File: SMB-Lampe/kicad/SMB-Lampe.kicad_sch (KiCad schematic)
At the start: 2 parts, among them SW1 SW_SPST, U1 MOUDLE-SEEEDUINO-XIAO-ESP32C3

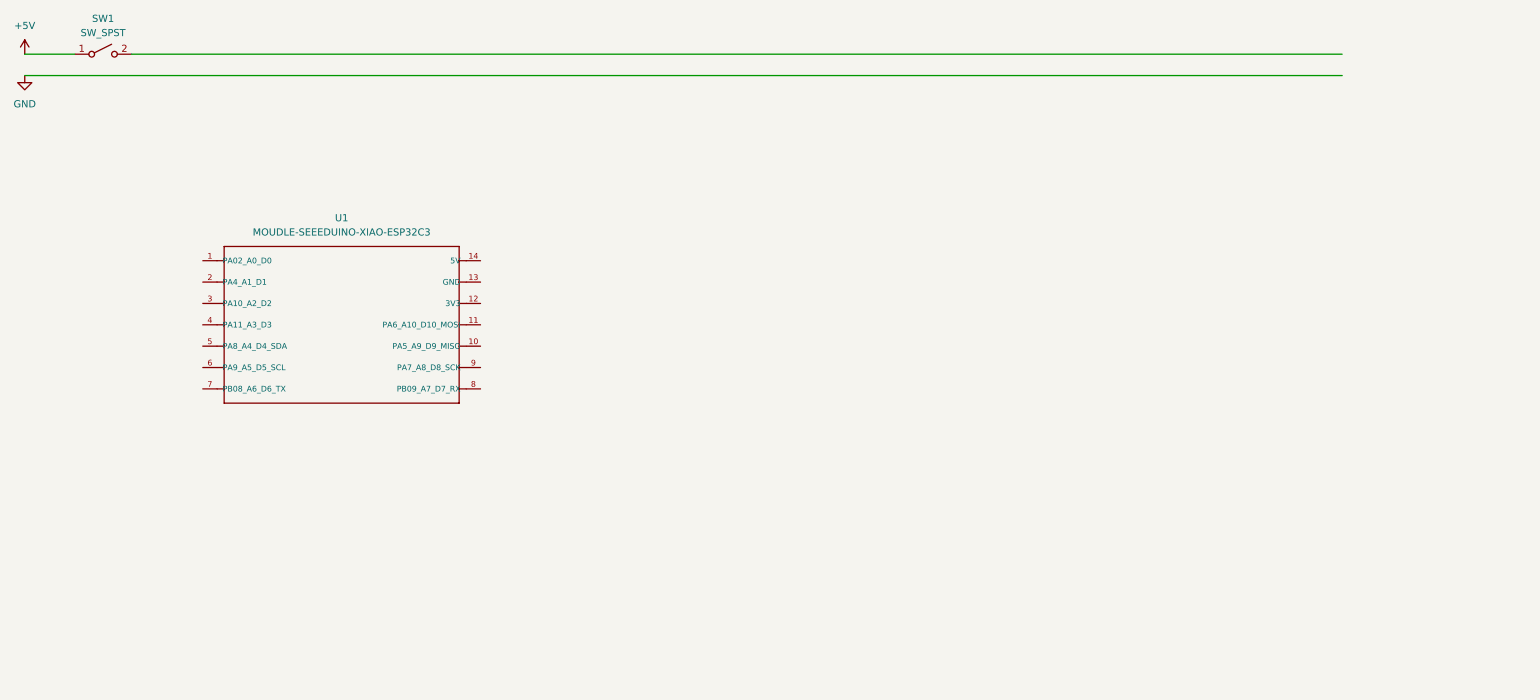
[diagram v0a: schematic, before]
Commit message: Spannungsversorgung zu ESP hinzugefügt
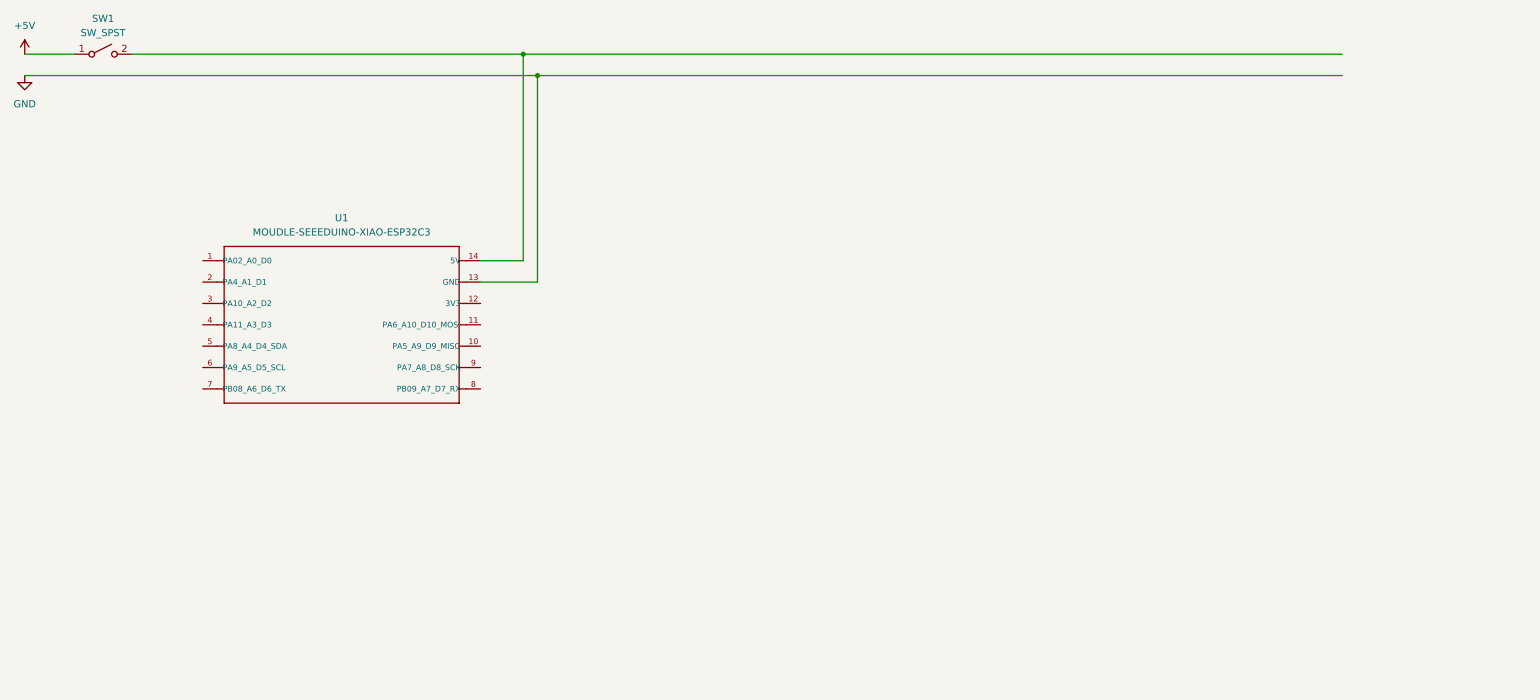
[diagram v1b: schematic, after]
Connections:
- net GND: now also U1.13 (GND)
- net at SW1.2 (B): now also U1.14 (5V)
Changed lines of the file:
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@@
 	(generator_version "9.0")
 	(paper "A4")
+	(junction
+		(at 116.84 29.21)
+		(diameter 0)
+		(color 0 0 0 0)
+	)
+	(junction
+		(at 114.3 25.4)
+		(diameter 0)
+		(color 0 0 0 0)
+	)
 	(wire
 		(pts
@@
 	(wire
 		(pts
-			(xy 25.4 29.21) (xy 260.35 29.21)
+			(xy 114.3 25.4) (xy 114.3 62.23)
 		)
 		(stroke
@@
 	(wire
 		(pts
-			(xy 44.45 25.4) (xy 260.35 25.4)
+			(xy 106.68 66.04) (xy 116.84 66.04)
 		)
 		(stroke
+			(width 0)
+			(type default)
+		)
+	)
+	(wire
+		(pts
+			(xy 116.84 29.21) (xy 260.35 29.21)
+		)
+		(stroke
+			(width 0)
+			(type default)
+		)
+	)
+	(wire
+		(pts
+			(xy 25.4 29.21) (xy 116.84 29.21)
+		)
+		(stroke
+			(width 0)
+			(type default)
+		)
+	)
+	(wire
+		(pts
+			(xy 44.45 25.4) (xy 114.3 25.4)
+		)
+		(stroke
+			(width 0)
+			(type default)
+		)
+	)
+	(wire
+		(pts
+			(xy 106.68 62.23) (xy 114.3 62.23)
+		)
+		(stroke
+			(width 0)
+			(type default)
+		)
+	)
+	(wire
+		(pts
+			(xy 114.3 25.4) (xy 260.35 25.4)
+		)
+		(stroke
+			(width 0)
+			(type default)
+		)
+	)
+	(wire
+		(pts
+			(xy 116.84 29.21) (xy 116.84 66.04)
+		)
+		(stroke

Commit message: Beidseitige Platine Für hinteres Hinterbein
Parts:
- removed U1: MOUDLE-SEEEDUINO-XIAO-ESP32C3, xiao ESP32C3_PCB:MOUDLE14P-SMD-2.54-21X17.8MM, symbol MOUDLE-SEEEDUINO-XIAO-ESP32C3:MOUDLE-SEEEDUINO-XIAO-ESP32C3
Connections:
- net Hinterbein_hinten_Seite1_LED-P/+5V: now reaches SW1.2 (B)
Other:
- added sheet Hauptplatine (Hauptplatine/Hauptplatine.kicad_sch)
- added sheet Hinterbein_hinten_Seite1_LED-P (Hinterbein_hinten_Seite1_LED-P/Hinterbein_hinten_Seite1_LED-P.kicad_sch)
- added sheet Hinterbein_vorne_Seite1_LED-P (Hinterbein_vorne_Seite1_LED-P/Hinterbein_vorne_Seite1_LED-P.kicad_sch)
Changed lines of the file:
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@@
 	(paper "A4")
 	(junction
-		(at 116.84 29.21)
+		(at 101.6 25.4)
 		(diameter 0)
 		(color 0 0 0 0)
 	)
 	(junction
-		(at 114.3 25.4)
+		(at 110.49 58.42)
 		(diameter 0)
 		(color 0 0 0 0)
@@
 	(wire
 		(pts
+			(xy 101.6 25.4) (xy 260.35 25.4)
+		)
+		(stroke
+			(width 0)
+			(type default)
+		)
+	)
+	(wire
+		(pts
 			(xy 25.4 25.4) (xy 34.29 25.4)
 		)
@@
 	(wire
 		(pts
-			(xy 114.3 25.4) (xy 114.3 62.23)
-		)
-		(stroke
-			(width 0)
-			(type default)
-		)
-	)
-	(wire
-		(pts
-			(xy 106.68 66.04) (xy 116.84 66.04)
-		)
-		(stroke
-			(width 0)
-			(type default)
-		)
-	)
-	(wire
-		(pts
-			(xy 116.84 29.21) (xy 260.35 29.21)
-		)
-		(stroke
-			(width 0)
-			(type default)
-		)
-	)
-	(wire
-		(pts
-			(xy 25.4 29.21) (xy 116.84 29.21)
-		)
-		(stroke
-			(width 0)
-			(type default)
-		)
-	)
-	(wire
-		(pts
-			(xy 44.45 25.4) (xy 114.3 25.4)
-		)
-		(stroke
-			(width 0)
-			(type default)
-		)
-	)
-	(wire
-		(pts
-			(xy 106.68 62.23) (xy 114.3 62.23)
-		)
-		(stroke
-			(width 0)
-			(type default)
-		)
-	)
-	(wire
-		(pts
-			(xy 114.3 25.4) (xy 260.35 25.4)
-		)
-		(stroke
-			(width 0)
-			(type default)
-		)
-	)
-	(wire
-		(pts
-			(xy 116.84 29.21) (xy 116.84 66.04)
+			(xy 101.6 25.4) (xy 101.6 58.42)
+		)
+		(stroke
+			(width 0)
+			(type default)
+		)
+	)
+	(wire
+		(pts
+			(xy 25.4 29.21) (xy 260.35 29.21)
+		)
+		(stroke
+			(width 0)
+			(type default)
+		)
+	)
+	(wire
+		(pts
+			(xy 110.49 58.42) (xy 111.76 58.42)
+		)
+		(stroke
+			(width 0)
+			(type default)
+		)
+	)
+	(wire
+		(pts
+			(xy 44.45 25.4) (xy 101.6 25.4)
+		)
+		(stroke
+			(width 0)
+			(type default)
+		)
+	)
+	(wire
+		(pts
+			(xy 101.6 58.42) (xy 110.49 58.42)
 		)
 		(stroke
@@
 		)
 	)
-	(symbol
-		(lib_id "MOUDLE-SEEEDUINO-XIAO-ESP32C3:MOUDLE-SEEEDUINO-XIAO-ESP32C3")
-		(at 82.55 73.66 0)
-		(unit 1)
-		(exclude_from_sim no)
-		(in_bom yes)
-		(on_board yes)
-		(dnp no)
-		(fields_autoplaced yes)
-		(property "Reference" "U1"
-			(at 81.915 54.61 0)
-			(effects
-				(font
-					(size 1.27 1.27)
-				)
-			)
-		)
-		(property "Value" "MOUDLE-SEEEDUINO-XIAO-ESP32C3"
-			(at 81.915 57.15 0)
-			(effects
-				(font
-					(size 1.27 1.27)
-				)
-			)
-		)
-		(property "Footprint" "xiao ESP32C3_PCB:MOUDLE14P-SMD-2.54-21X17.8MM"
-			(at 82.55 73.66 0)
-			(effects
-				(font
-					(size 1.27 1.27)
-				)
-				(justify bottom)
-				(hide yes)
-			)
-		)
-		(property "Datasheet" ""
-			(at 82.55 73.66 0)
-			(effects
-				(font
-					(size 1.27 1.27)
-				)
-				(hide yes)
-			)
-		)
-		(property "Description" ""
-			(at 82.55 73.66 0)
-			(effects
-				(font
-					(size 1.27 1.27)
-				)
-				(hide yes)
-			)
-		)
-		(pin "14"
-		)
-		(pin "10"
-		)
-		(pin "4"
-		)
-		(pin "12"
-		)
-		(pin "13"
-		)
-		(pin "2"
-		)
-		(pin "3"
-		)
-		(pin "5"
-		)
-		(pin "7"
-		)
-		(pin "8"
-		)
-		(pin "9"
-		)
-		(pin "6"
-		)
-		(pin "1"
-		)
-		(pin "11"
-		)
-		(instances
-			(project ""
-				(path "/4831ca1b-de6c-4f01-b2f4-c7955e9e85c5"
-					(reference "U1")
-					(unit 1)
-				)
-			)
+	(sheet
+		(at 110.49 52.07)
+		(size 34.29 34.29)
+		(exclude_from_sim no)
+		(in_bom yes)
+		(on_board yes)
+		(dnp no)
+		(fields_autoplaced yes)
+		(stroke
+			(width 0.1524)
+			(type solid)
+		)
+		(fill
+			(color 0 0 0 0.0000)
+		)
+		(property "Sheetname" "Hinterbein_hinten_Seite1_LED-P"
+			(at 110.49 51.3584 0)
+			(effects
+				(font
+					(size 1.27 1.27)
+				)
+				(justify left bottom)
+			)
+		)
+		(property "Sheetfile" "Hinterbein_hinten_Seite1_LED-P/Hinterbein_hinten_Seite1_LED-P.kicad_sch"
+			(at 110.49 86.9446 0)
+			(effects
+				(font
+					(size 1.27 1.27)
+				)
+				(justify left top)
+				(hide yes)
+			)
+		)
+		(pin "+5V" input
+			(at 110.49 58.42 180)
+			(effects
+				(font
+					(size 1.27 1.27)
+					(thickness 0.1588)
+				)
+				(justify left)
+			)
+		)
+		(pin "GND" input
+			(at 110.49 63.5 180)
+			(effects
+				(font
+					(size 1.27 1.27)
+				)
+				(justify left)
+			)
+		)
+		(instances
+			(project "SMB-Lampe"
+				(path "/4831ca1b-de6c-4f01-b2f4-c7955e9e85c5"
+					(page "3")
+				)
+			)
+		)
+	)
+	(sheet
+		(at 60.96 52.07)
+		(size 27.94 34.29)
+		(exclude_from_sim no)
+		(in_bom yes)
+		(on_board yes)
+		(dnp no)
+		(fields_autoplaced yes)
+		(stroke
+			(width 0.254)
+			(type solid)
+			(color 111 255 74 1)
+		)
+		(fill
+			(color 0 0 0 0.0000)
+		)
+		(property "Sheetname" "Hauptplatine"
+			(at 60.96 51.3076 0)
+			(effects
+				(font
+					(size 1.27 1.27)
+				)
+				(justify left bottom)
+			)
+		)
+		(property "Sheetfile" "Hauptplatine/Hauptplatine.kicad_sch"
+			(at 60.96 86.9954 0)
+			(effects
+				(font
+					(size 1.27 1.27)
+				)
+				(justify left top)
+				(hide yes)
+			)
+		)
+		(instances
+			(project "SMB-Lampe"
+				(path "/4831ca1b-de6c-4f01-b2f4-c7955e9e85c5"
+					(page "2")
+				)
+			)
+		)
+	)
+	(sheet
+		(at 152.4 50.8)
+		(size 25.4 35.56)
+		(exclude_from_sim no)
+		(in_bom yes)
+		(on_board yes)
+		(dnp no)
+		(fields_autoplaced yes)
+		(stroke
+			(width 0.1524)
+			(type solid)
+		)
+		(fill
+			(color 0 0 0 0.0000)
+		)
+		(property "Sheetname" "Hinterbein_vorne_Seite1_LED-P"
+			(at 152.4 50.0884 0)
+			(effects
+				(font
+					(size 1.27 1.27)
+				)
+				(justify left bottom)
+			)
+		)
+		(property "Sheetfile" "Hinterbein_vorne_Seite1_LED-P/Hinterbein_vorne_Seite1_LED-P.kicad_sch"
+			(at 152.4 86.9446 0)
+			(effects
+				(font
+					(size 1.27 1.27)
+				)
+				(justify left top)
+				(hide yes)
+			)
+		)
+		(instances
+			(project "SMB-Lampe"
+				(path "/4831ca1b-de6c-4f01-b2f4-c7955e9e85c5"
+					(page "4")
+				)
+			)

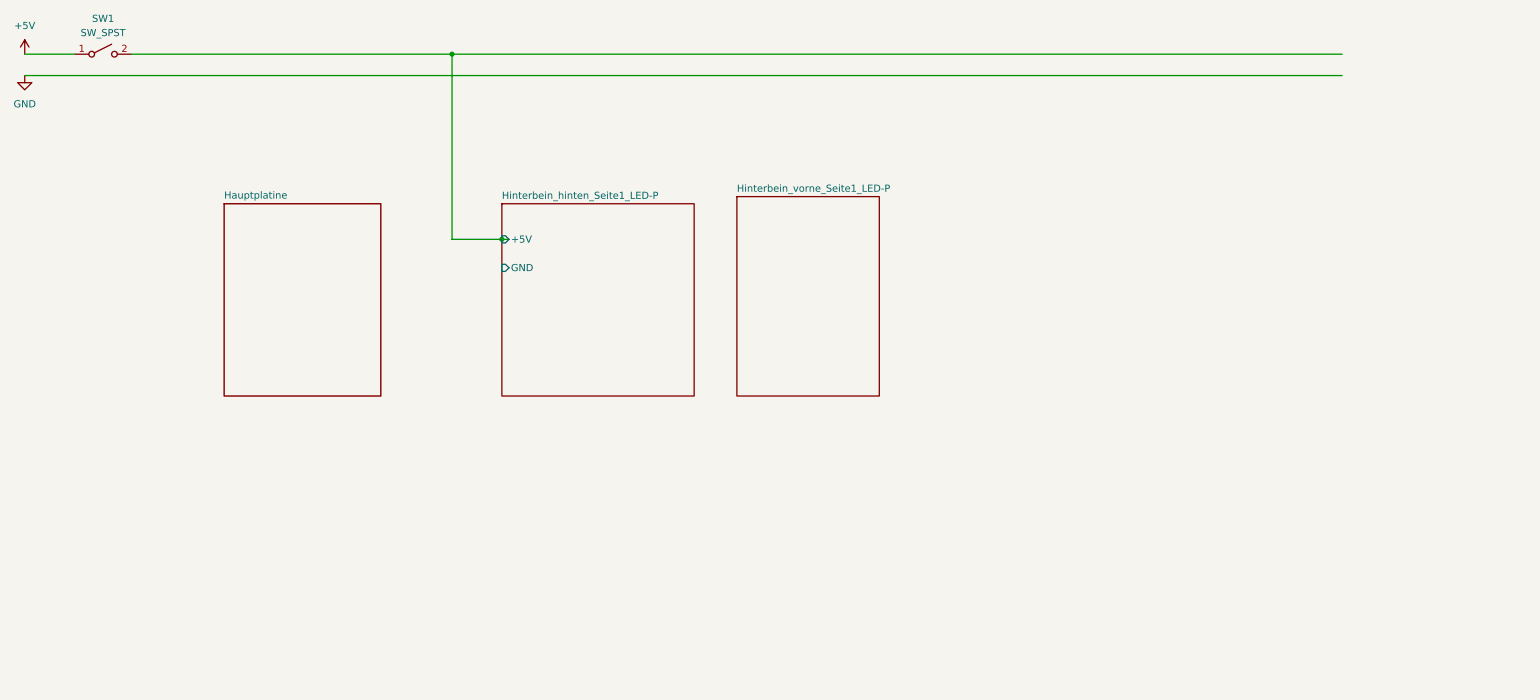
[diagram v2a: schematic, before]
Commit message: Hauptplatine skizziert
Bezeichner stimmen noch nicht
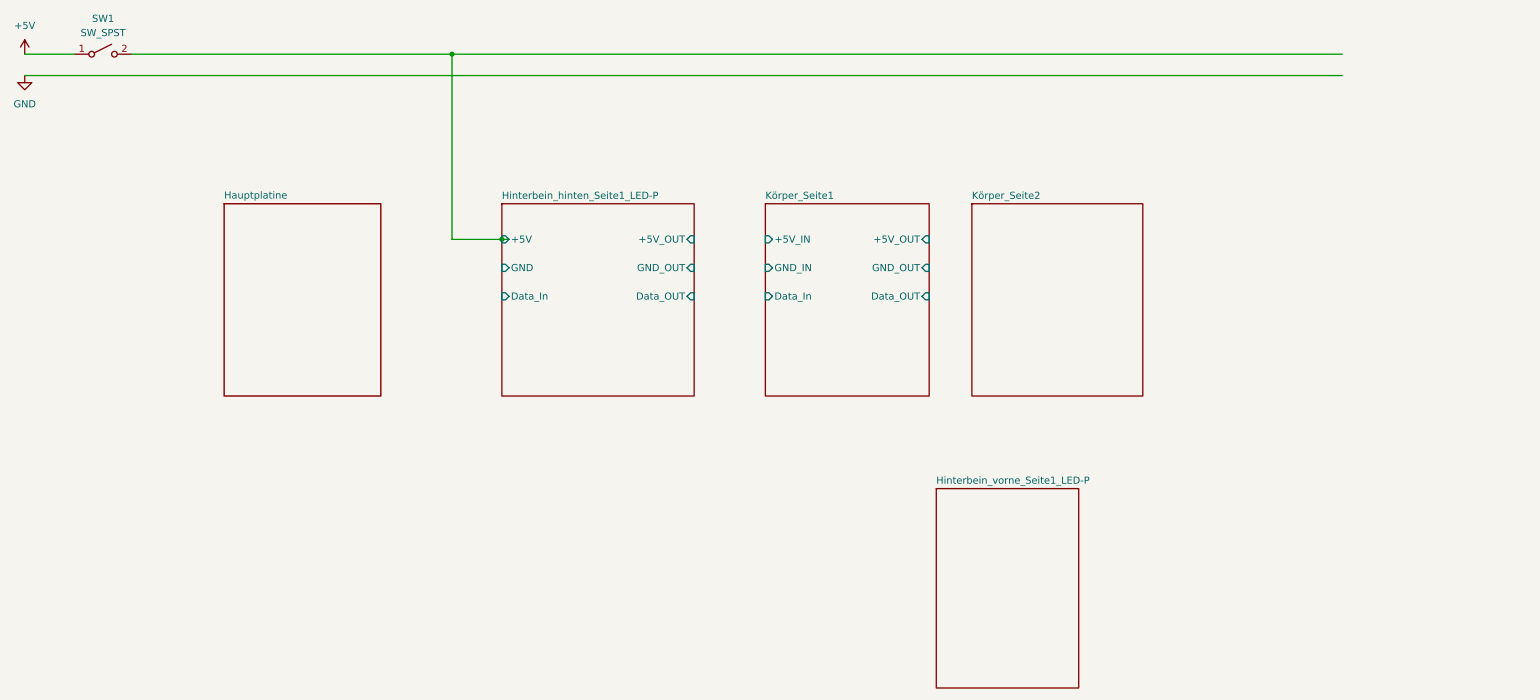
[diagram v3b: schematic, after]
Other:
- added sheet Körper_Seite1 (Körper_Seite1/KörperKörper_Seite1.kicad_sch)
- added sheet Körper_Seite2 (Körper_Seite2/Körper_Seite2.kicad_sch)
- sheet Hinterbein_hinten_Seite1_LED-P ports: added +5V_OUT, Data_In, Data_OUT, GND_OUT; removed none
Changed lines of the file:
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@@
+			)
+		)
+		(pin "+5V_OUT" input
+			(at 144.78 58.42 0)
+			(effects
+				(font
+					(size 1.27 1.27)
+				)
+				(justify right)
+			)
+		)
+		(pin "Data_In" input
+			(at 110.49 68.58 180)
+			(effects
+				(font
+					(size 1.27 1.27)
+				)
+				(justify left)
+			)
+		)
+		(pin "Data_OUT" input
+			(at 144.78 68.58 0)
+			(effects
+				(font
+					(size 1.27 1.27)
+				)
+				(justify right)
+			)
+		)
+		(pin "GND_OUT" input
+			(at 144.78 63.5 0)
+			(effects
+				(font
+					(size 1.27 1.27)
+				)
+				(justify right)
 			)
 		)
@@
 	)
 	(sheet
-		(at 152.4 50.8)
+		(at 187.96 102.87)
 		(size 25.4 35.56)
 		(exclude_from_sim no)
@@
 		)
 		(property "Sheetname" "Hinterbein_vorne_Seite1_LED-P"
-			(at 152.4 50.0884 0)
+			(at 187.96 102.1584 0)
 			(effects
 				(font
@@
 		)
 		(property "Sheetfile" "Hinterbein_vorne_Seite1_LED-P/Hinterbein_vorne_Seite1_LED-P.kicad_sch"
-			(at 152.4 86.9446 0)
+			(at 187.96 139.0146 0)
 			(effects
 				(font
@@
 				)
 			)
+		)
+	)
+	(sheet
+		(at 157.48 52.07)
+		(size 29.21 34.29)
+		(exclude_from_sim no)
+		(in_bom yes)
+		(on_board yes)
+		(dnp no)
+		(fields_autoplaced yes)
+		(stroke
+			(width 0.1524)
+			(type solid)
+		)
+		(fill
+			(color 0 0 0 0.0000)
+		)
+		(property "Sheetname" "Körper_Seite1"
+			(at 157.48 51.3584 0)
+			(effects
+				(font
+					(size 1.27 1.27)
+				)
+				(justify left bottom)
+			)
+		)
+		(property "Sheetfile" "Körper_Seite1/KörperKörper_Seite1.kicad_sch"
+			(at 157.48 86.9446 0)
+			(effects
+				(font
+					(size 1.27 1.27)
+				)
+				(justify left top)
+				(hide yes)
+			)
+		)
+		(pin "+5V_IN" input
+			(at 157.48 58.42 180)
+			(effects
+				(font
+					(size 1.27 1.27)
+				)
+				(justify left)
+			)
+		)
+		(pin "+5V_OUT" input
+			(at 186.69 58.42 0)
+			(effects
+				(font
+					(size 1.27 1.27)
+				)
+				(justify right)
+			)
+		)
+		(pin "Data_In" input
+			(at 157.48 68.58 180)
+			(effects
+				(font
+					(size 1.27 1.27)
+				)
+				(justify left)
+			)
+		)
+		(pin "Data_OUT" input
+			(at 186.69 68.58 0)
+			(effects
+				(font
+					(size 1.27 1.27)
+				)
+				(justify right)
+			)
+		)
+		(pin "GND_OUT" input
+			(at 186.69 63.5 0)
+			(effects
+				(font
+					(size 1.27 1.27)
+				)
+				(justify right)
+			)
+		)
+		(pin "GND_IN" input
+			(at 157.48 63.5 180)
+			(effects
+				(font
+					(size 1.27 1.27)
+				)
+				(justify left)
+			)
+		)
+		(instances
+			(project "SMB-Lampe"
+				(path "/4831ca1b-de6c-4f01-b2f4-c7955e9e85c5"
+					(page "5")
+				)
+			)
+		)
+	)
+	(sheet
+		(at 194.31 52.07)
+		(size 30.48 34.29)
+		(exclude_from_sim no)
+		(in_bom yes)
+		(on_board yes)
+		(dnp no)
+		(fields_autoplaced yes)
+		(stroke
+			(width 0.1524)
+			(type solid)
+		)
+		(fill
+			(color 0 0 0 0.0000)
+		)
+		(property "Sheetname" "Körper_Seite2"
+			(at 194.31 51.3584 0)
+			(effects
+				(font
+					(size 1.27 1.27)
+				)
+				(justify left bottom)
+			)
+		)
+		(property "Sheetfile" "Körper_Seite2/Körper_Seite2.kicad_sch"
+			(at 194.31 86.9446 0)
+			(effects
+				(font
+					(size 1.27 1.27)
+				)
+				(justify left top)
+				(hide yes)
+			)
+		)
+		(instances
+			(project "SMB-Lampe"
+				(path "/4831ca1b-de6c-4f01-b2f4-c7955e9e85c5"
+					(page "6")
+				)
+			)
